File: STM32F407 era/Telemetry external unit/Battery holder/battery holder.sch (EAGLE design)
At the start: 1 part

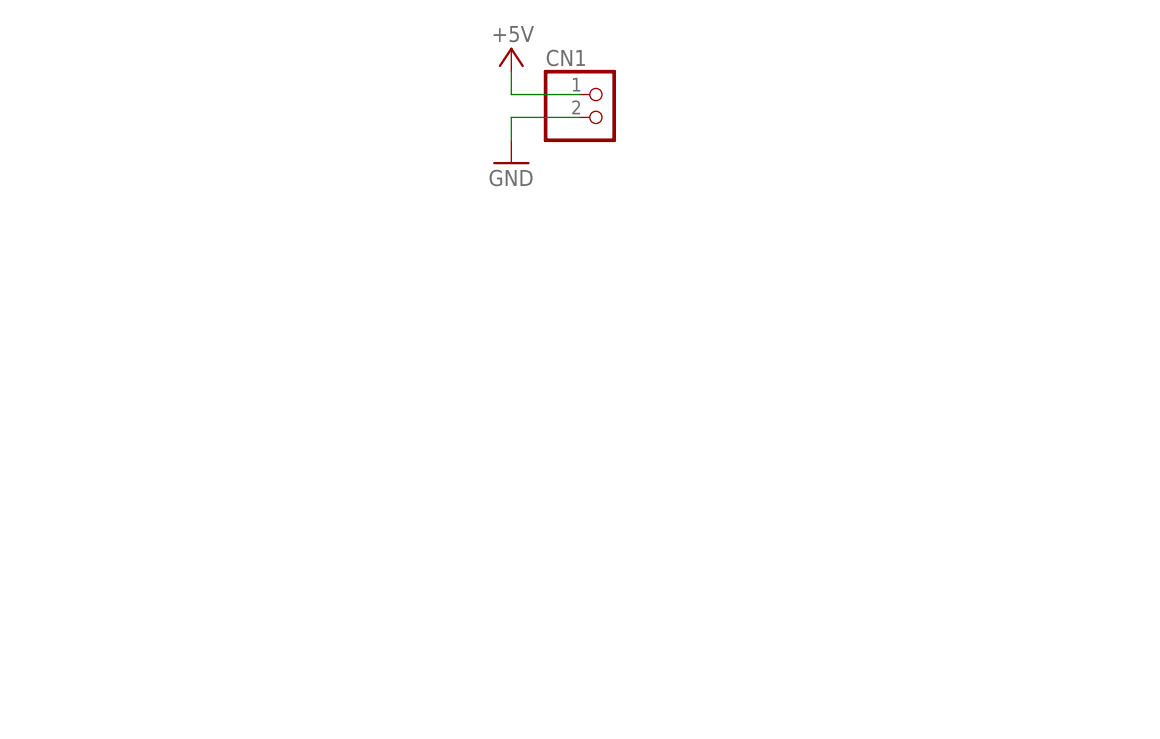
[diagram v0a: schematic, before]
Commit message: changes to battery board
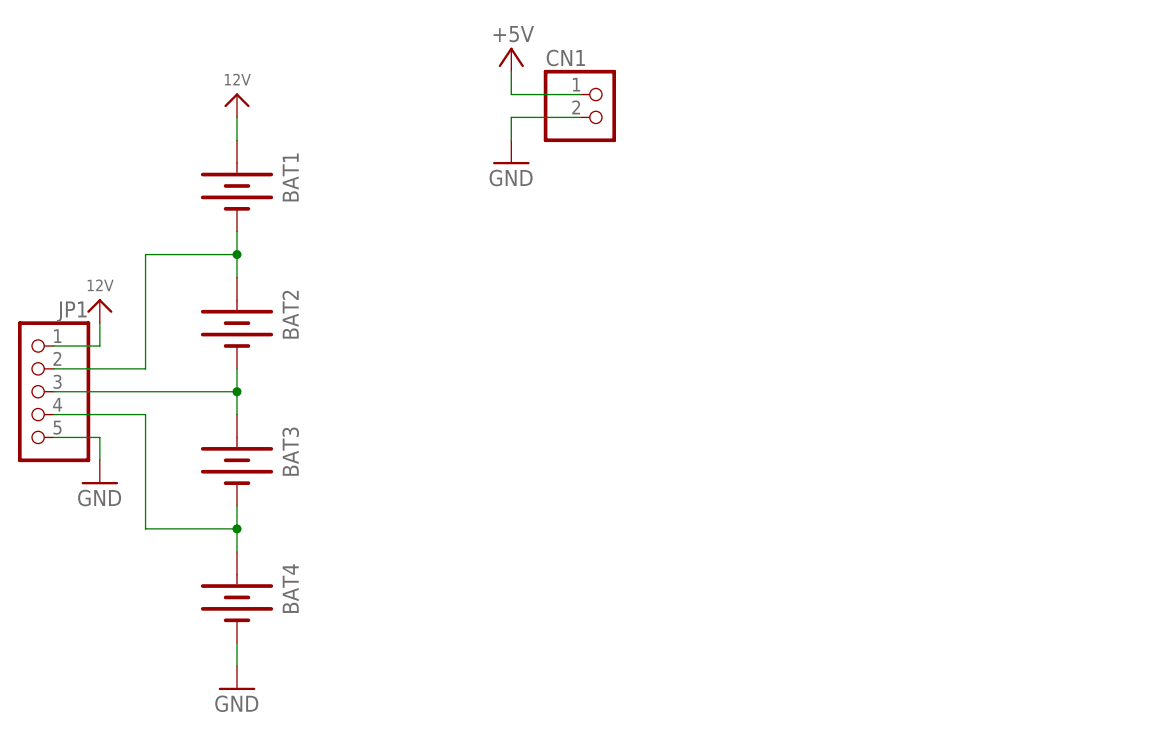
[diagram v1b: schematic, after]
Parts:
- added BAT1, BAT2, BAT3, BAT4: (no value), SparkFun-Electromechanical:BATTERY18650
- added JP1: (no value), pinhead:PINHD-1X5/90
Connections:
- new net 12V: BAT1.+, JP1.1
- new net N$1: BAT1.-, BAT2.+, JP1.2
- new net N$2: BAT2.-, BAT3.+, JP1.3
- new net N$3: BAT3.-, BAT4.+, JP1.4
- net GND: now also BAT4.-, JP1.5
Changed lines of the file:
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@@
 <part name="P+2" library="supply1" deviceset="+5V" device=""/>
 <part name="GND6" library="supply1" deviceset="GND" device=""/>
+<part name="BAT1" library="SparkFun-Electromechanical" deviceset="BATTERY" device="18650"/>
+<part name="BAT2" library="SparkFun-Electromechanical" deviceset="BATTERY" device="18650"/>
+<part name="BAT3" library="SparkFun-Electromechanical" deviceset="BATTERY" device="18650"/>
+<part name="BAT4" library="SparkFun-Electromechanical" deviceset="BATTERY" device="18650"/>
+<part name="JP1" library="pinhead" deviceset="PINHD-1X5" device="/90"/>
+<part name="U$1" library="microbuilder" deviceset="12V" device=""/>
+<part name="U$2" library="microbuilder" deviceset="12V" device=""/>
+<part name="GND1" library="supply1" deviceset="GND" device=""/>
+<part name="GND2" library="supply1" deviceset="GND" device=""/>
 </parts>
 <sheets>
@@
 </instance>
 <instance part="GND6" gate="1" x="129.54" y="68.58"/>
+<instance part="BAT1" gate="G$1" x="99.06" y="66.04" rot="R270"/>
+<instance part="BAT2" gate="G$1" x="99.06" y="50.8" rot="R270"/>
+<instance part="BAT3" gate="G$1" x="99.06" y="35.56" rot="R270"/>
+<instance part="BAT4" gate="G$1" x="99.06" y="20.32" rot="R270"/>
+<instance part="JP1" gate="A" x="76.2" y="43.18" rot="MR0"/>
+<instance part="U$1" gate="G$1" x="99.06" y="76.2"/>
+<instance part="U$2" gate="G$1" x="83.82" y="53.34"/>
+<instance part="GND1" gate="1" x="99.06" y="10.16"/>
+<instance part="GND2" gate="1" x="83.82" y="33.02"/>
 </instances>
 <busses>
@@
 <wire x1="129.54" y1="73.66" x2="129.54" y2="71.12" width="0.1524" layer="91"/>
 </segment>
+<segment>
+<pinref part="JP1" gate="A" pin="5"/>
+<pinref part="GND2" gate="1" pin="GND"/>
+<wire x1="78.74" y1="38.1" x2="83.82" y2="38.1" width="0.1524" layer="91"/>
+<wire x1="83.82" y1="38.1" x2="83.82" y2="35.56" width="0.1524" layer="91"/>
+</segment>
+<segment>
+<pinref part="BAT4" gate="G$1" pin="-"/>
+<pinref part="GND1" gate="1" pin="GND"/>
+<wire x1="99.06" y1="15.24" x2="99.06" y2="12.7" width="0.1524" layer="91"/>
+</segment>
 </net>
 <net name="+5V" class="0">
@@
 </segment>
 </net>
+<net name="N$1" class="0">
+<segment>
+<pinref part="BAT1" gate="G$1" pin="-"/>
+<pinref part="BAT2" gate="G$1" pin="+"/>
+<wire x1="99.06" y1="60.96" x2="99.06" y2="58.42" width="0.1524" layer="91"/>
+<pinref part="JP1" gate="A" pin="2"/>
+<wire x1="99.06" y1="58.42" x2="99.06" y2="55.88" width="0.1524" layer="91"/>
+<wire x1="78.74" y1="45.72" x2="88.9" y2="45.72" width="0.1524" layer="91"/>
+<wire x1="88.9" y1="45.72" x2="88.9" y2="58.42" width="0.1524" layer="91"/>
+<wire x1="88.9" y1="58.42" x2="99.06" y2="58.42" width="0.1524" layer="91"/>
+<junction x="99.06" y="58.42"/>
+</segment>
+</net>
+<net name="N$2" class="0">
+<segment>
+<pinref part="BAT2" gate="G$1" pin="-"/>
+<pinref part="BAT3" gate="G$1" pin="+"/>
+<wire x1="99.06" y1="45.72" x2="99.06" y2="43.18" width="0.1524" layer="91"/>
+<pinref part="JP1" gate="A" pin="3"/>
+<wire x1="99.06" y1="43.18" x2="99.06" y2="40.64" width="0.1524" layer="91"/>
+<wire x1="78.74" y1="43.18" x2="99.06" y2="43.18" width="0.1524" layer="91"/>
+<junction x="99.06" y="43.18"/>
+</segment>
+</net>
+<net name="N$3" class="0">
+<segment>
+<pinref part="BAT3" gate="G$1" pin="-"/>
+<pinref part="BAT4" gate="G$1" pin="+"/>
+<wire x1="99.06" y1="30.48" x2="99.06" y2="27.94" width="0.1524" layer="91"/>
+<pinref part="JP1" gate="A" pin="4"/>
+<wire x1="99.06" y1="27.94" x2="99.06" y2="25.4" width="0.1524" layer="91"/>
+<wire x1="78.74" y1="40.64" x2="88.9" y2="40.64" width="0.1524" layer="91"/>
+<wire x1="88.9" y1="40.64" x2="88.9" y2="27.94" width="0.1524" layer="91"/>
+<wire x1="88.9" y1="27.94" x2="99.06" y2="27.94" width="0.1524" layer="91"/>
+<junction x="99.06" y="27.94"/>
+</segment>
+</net>
+<net name="12V" class="0">
+<segment>
+<pinref part="JP1" gate="A" pin="1"/>
+<pinref part="U$2" gate="G$1" pin="12V"/>
+<wire x1="78.74" y1="48.26" x2="83.82" y2="48.26" width="0.1524" layer="91"/>
+<wire x1="83.82" y1="48.26" x2="83.82" y2="50.8" width="0.1524" layer="91"/>
+</segment>
+<segment>
+<pinref part="U$1" gate="G$1" pin="12V"/>
+<pinref part="BAT1" gate="G$1" pin="+"/>
+<wire x1="99.06" y1="73.66" x2="99.06" y2="71.12" width="0.1524" layer="91"/>
+</segment>
+</net>

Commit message: added Switching power supply to telemtry battery board
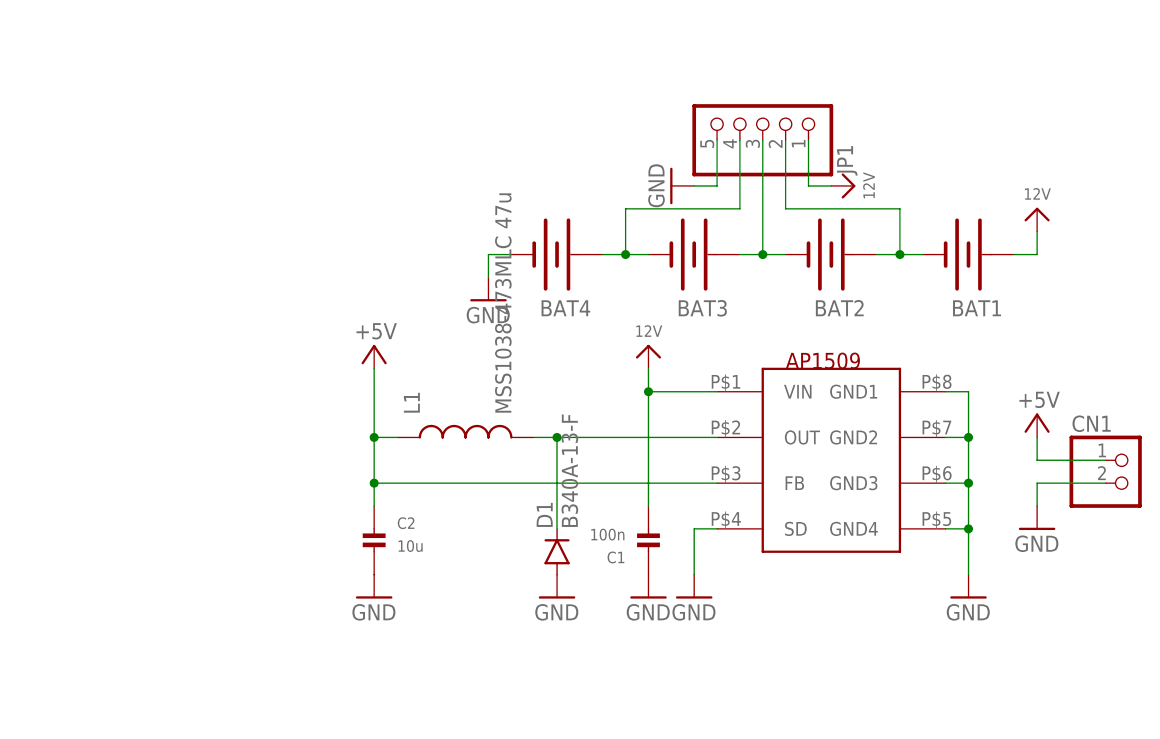
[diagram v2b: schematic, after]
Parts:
- added C1: 100n, microbuilder:CAP_CERAMIC_0603MP
- added C2: 10u, microbuilder:CAP_CERAMIC_0805MP
- added D1: B340A-13-F, SparkFun-DiscreteSemi:DIODESMA
- added L1: MSS1038-473MLC 47u, SparkFun-Passives:INDUCTORPWR
- added U$3: AP1509, unicorn_v2:AP1509
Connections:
- new net N$6: D1.C, L1.2, U$3.OUT
- net +5V: now also C2.P$1, L1.1, U$3.FB
- net 12V: now also C1.P$2, U$3.VIN
- net GND: now also C1.P$1, C2.P$2, D1.A, U$3.GND1, U$3.GND2, U$3.GND3, U$3.GND4, U$3.SD
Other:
- moved on the sheet: BAT1, BAT2, BAT3, BAT4, CN1, JP1
